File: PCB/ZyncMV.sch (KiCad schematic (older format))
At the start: 0 parts

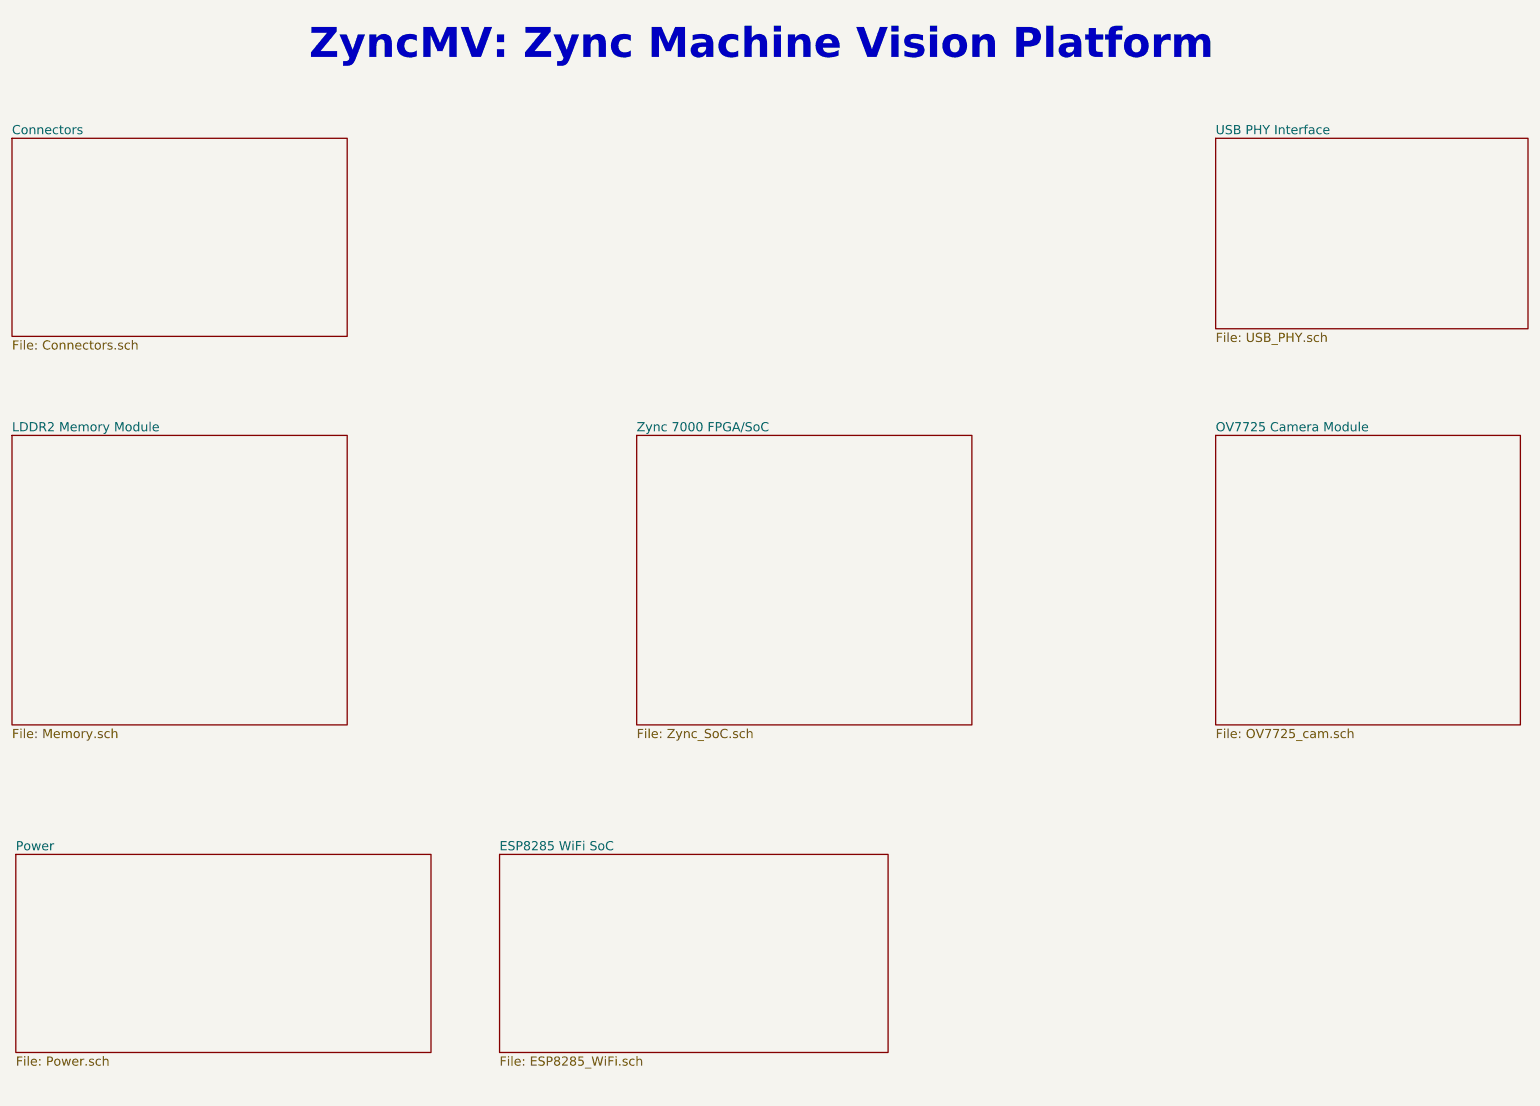
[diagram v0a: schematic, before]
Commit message: Progress
Datasheets added for regulators, regulators chosen, more datasheets
ralted to Zync 7000 added. Memory module chose footprint created and
datasheet added. Schematic work in progress. Project is slow going do to
th sheer amount of documenation to absorb on the Zync and makign high
pin count BGAs is tedious. More to follow soon.
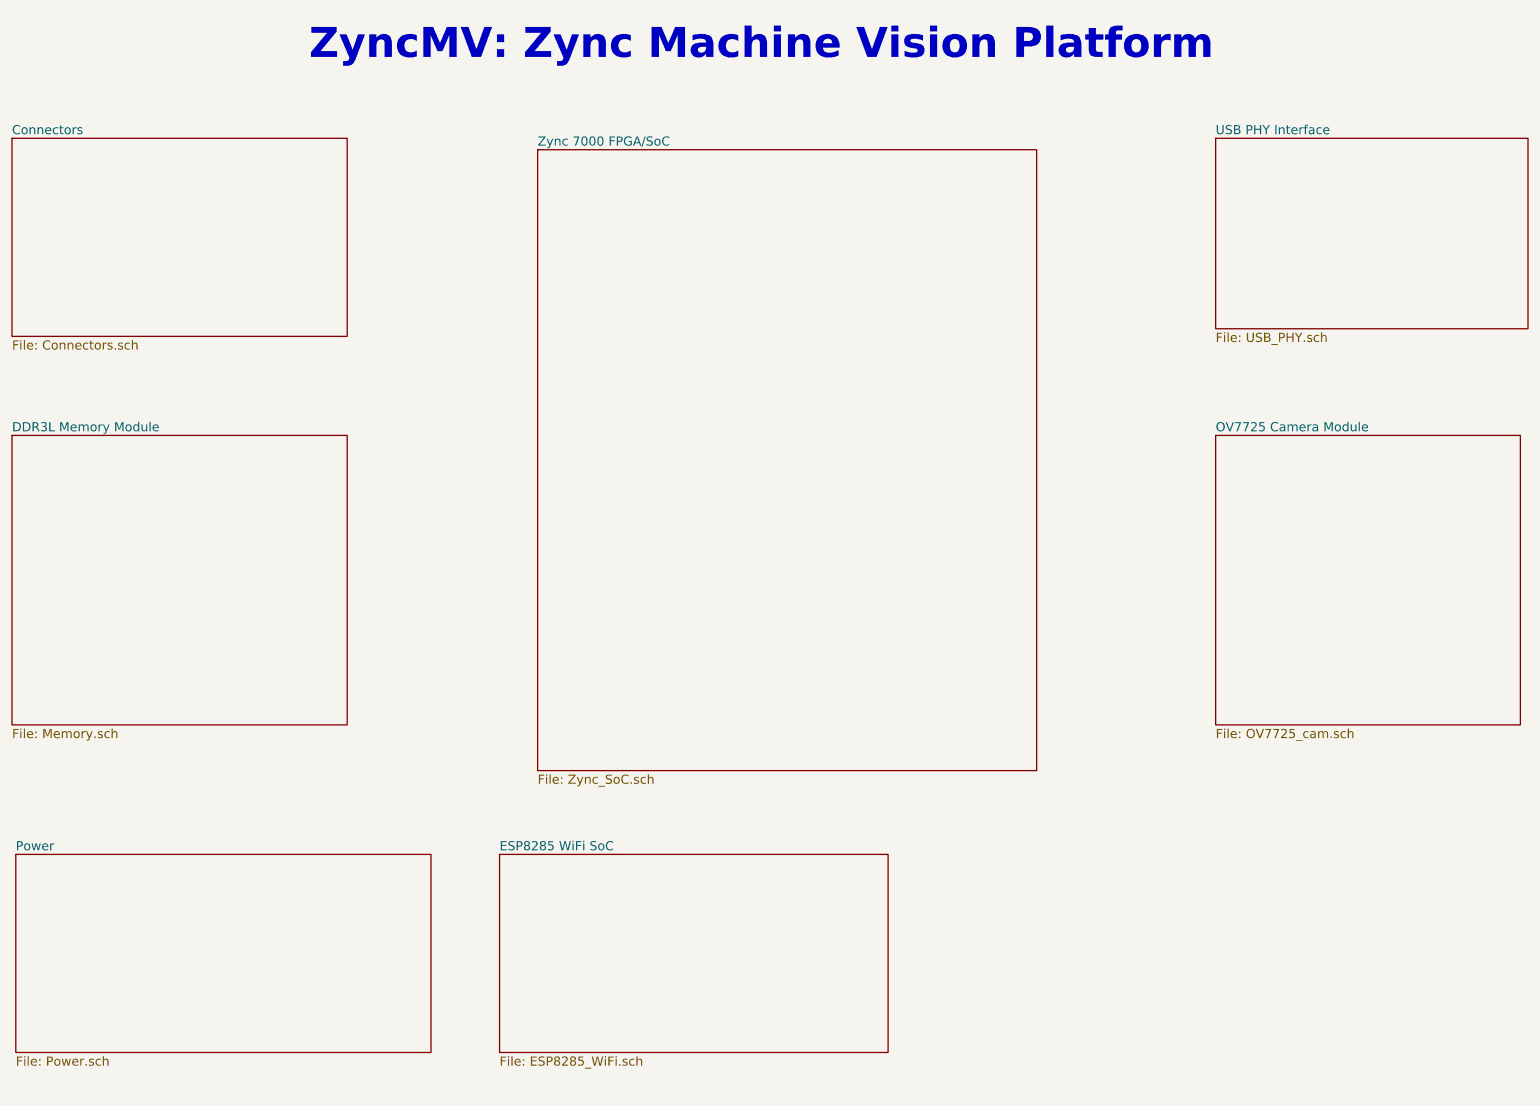
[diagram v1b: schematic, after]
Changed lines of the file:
@@
 LIBS:HydroPWNics_Lib
 LIBS:OnHand-Components-Sym
+LIBS:ZyncMV-cache
 EELAYER 25 0
 EELAYER END
 $Descr A4 11693 8268
 encoding utf-8
-Sheet 1 11
+Sheet 1 8
 Title ""
 Date ""
@@
 $EndDescr
 $Sheet
-S 5000 3450 2200 1900
+S 4350 1575 3275 4075
 U 585AE0B8
 F0 "Zync 7000 FPGA/SoC" 60
@@
 S 900  3450 2200 1900
 U 585AE128
-F0 "LDDR2 Memory Module" 60
+F0 "DDR3L Memory Module" 60
 F1 "Memory.sch" 60
 $EndSheet

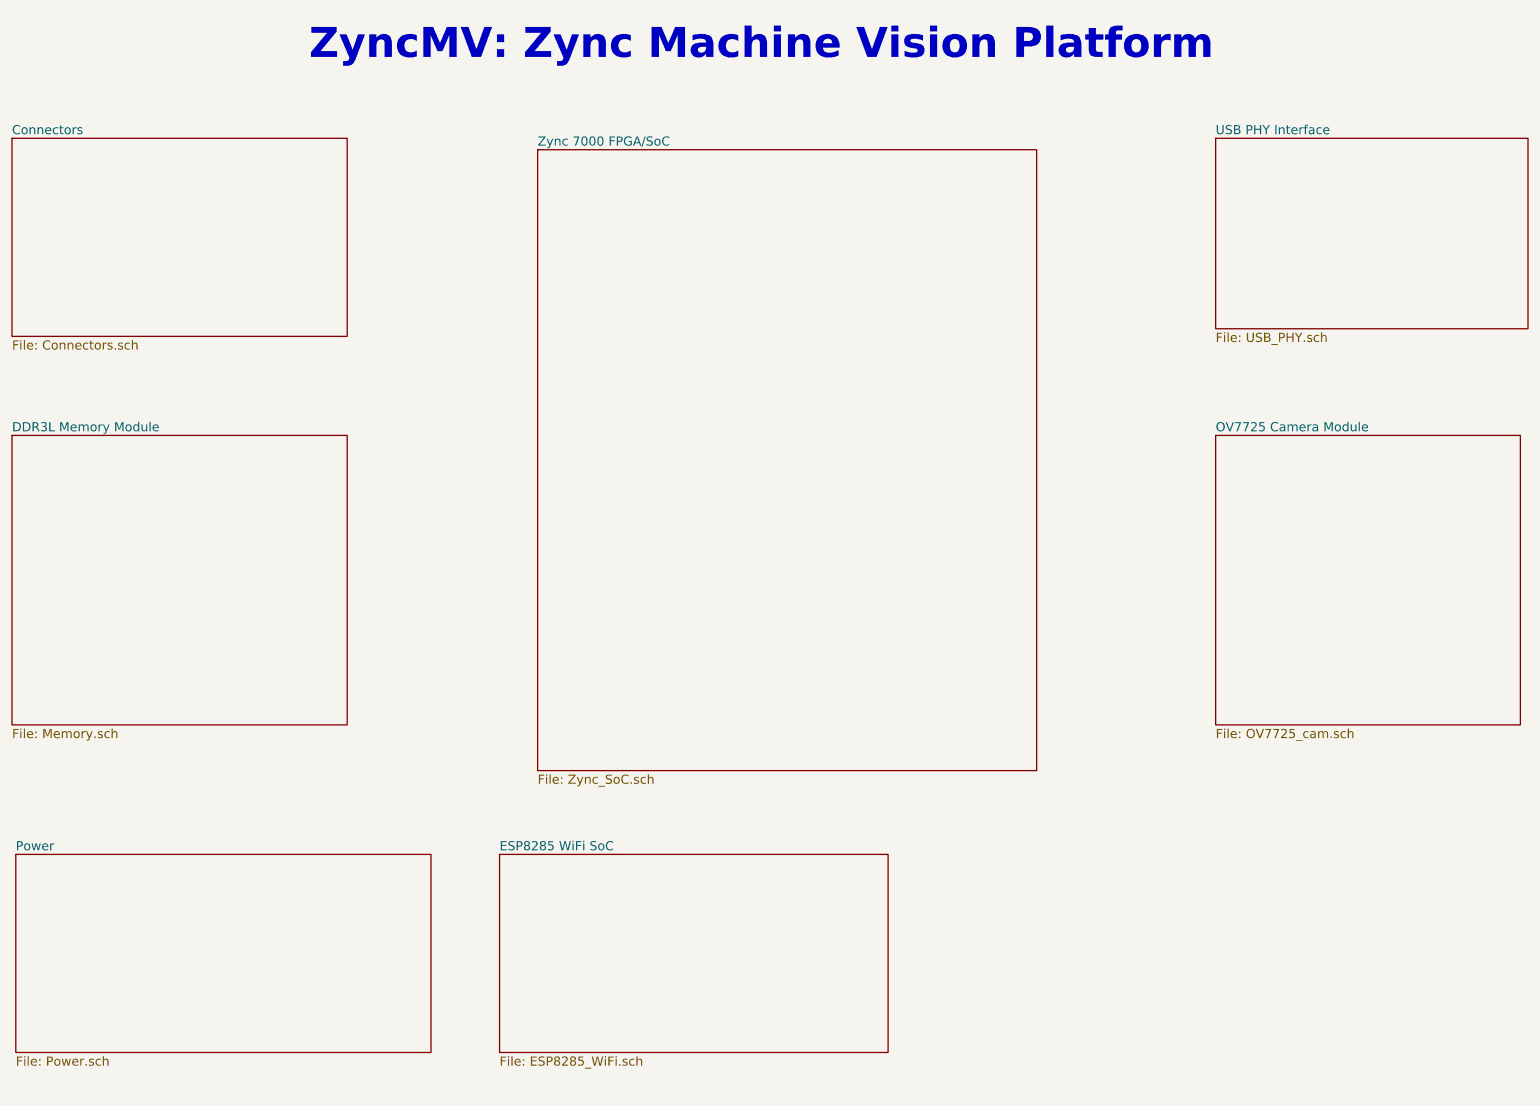
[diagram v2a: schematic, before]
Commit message: Power
Power topology change. Power system schematic spans 3 pages. two for the
PMIC that supplies the SoC and the DDR3L and an addional page covering
input stage and DCDC regulators for other voltages, particularly for the
off board lighting module.
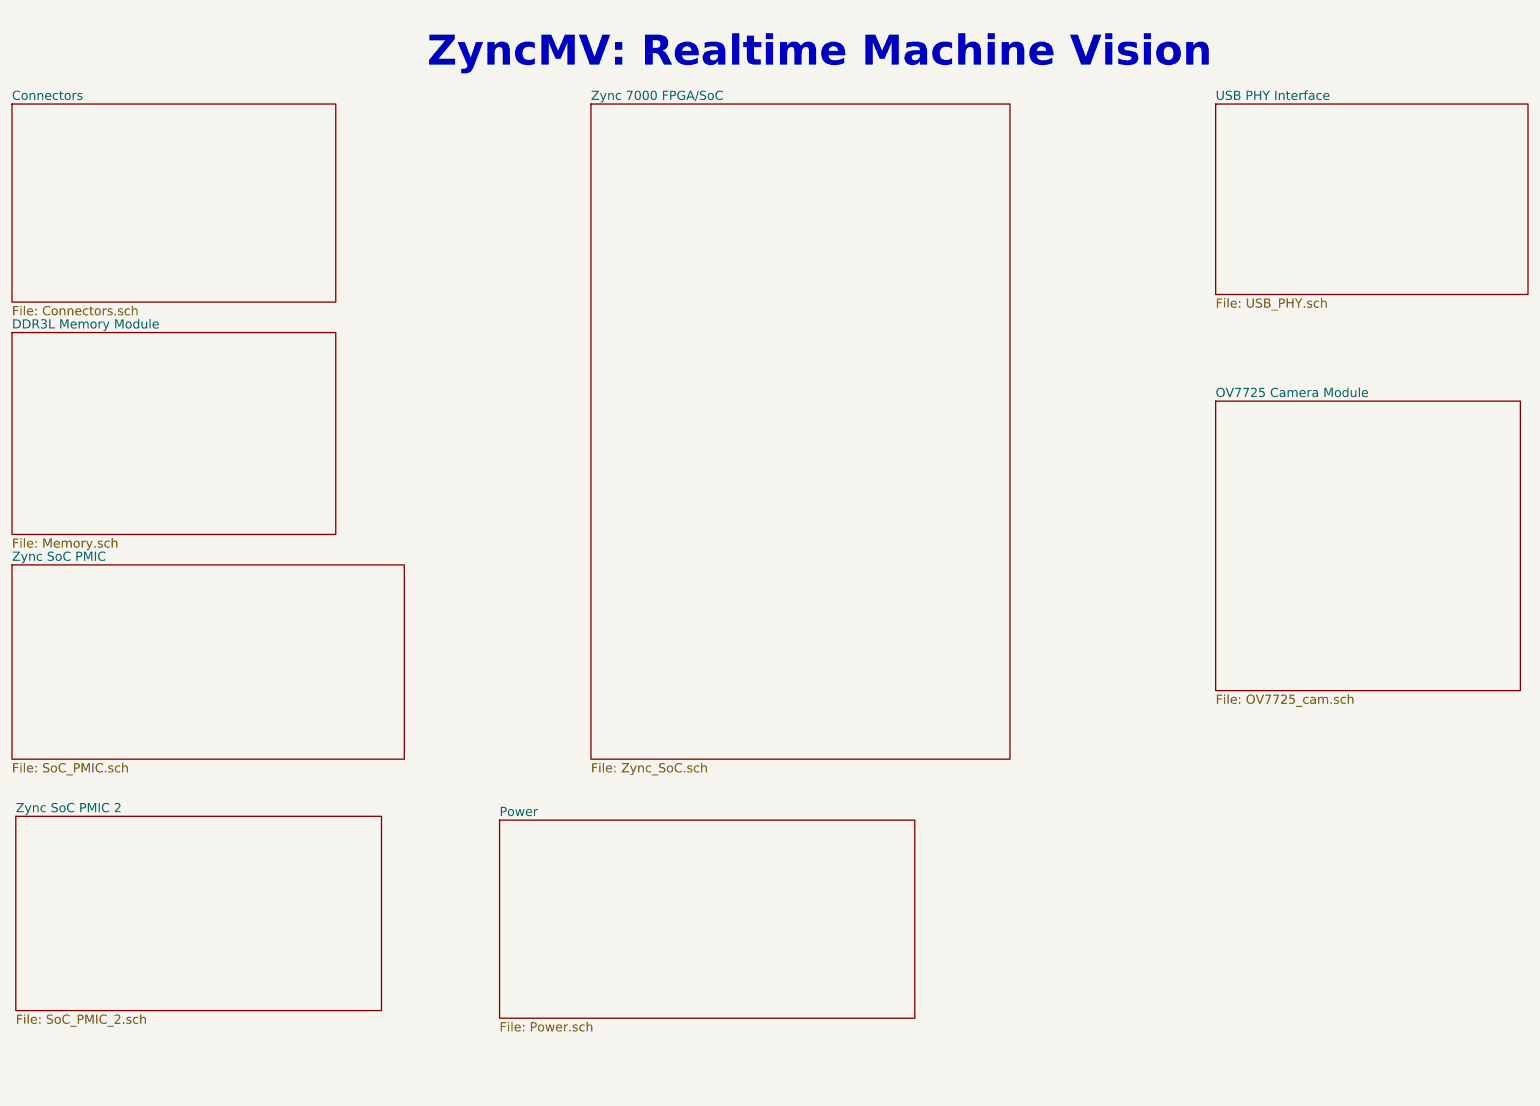
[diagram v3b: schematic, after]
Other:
- note added: "ZyncMV: Realtime Machine Vision"
- note removed: "ZyncMV: Zync Machine Vision Platform"
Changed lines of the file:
@@
 $Descr A4 11693 8268
 encoding utf-8
-Sheet 1 8
+Sheet 1 9
 Title ""
 Date "2016-12-23"
@@
 $EndDescr
 $Sheet
-S 4350 1575 3275 4075
+S 4700 1275 2750 4300
 U 585AE0B8
 F0 "Zync 7000 FPGA/SoC" 60
@@
 $EndSheet
 $Sheet
-S 925  6200 2725 1300
+S 4100 5975 2725 1300
 U 585AE0DE
 F0 "Power" 60
@@
 $EndSheet
 $Sheet
-S 8800 3450 2000 1900
+S 8800 3225 2000 1900
 U 585AE0EB
 F0 "OV7725 Camera Module" 60
@@
 $EndSheet
 $Sheet
-S 4100 6200 2550 1300
-U 585AE108
-F0 "ESP8285 WiFi SoC" 60
-F1 "ESP8285_WiFi.sch" 60
-$EndSheet
-$Sheet
-S 900  3450 2200 1900
+S 900  2775 2125 1325
 U 585AE128
 F0 "DDR3L Memory Module" 60
@@
 $EndSheet
 $Sheet
-S 900  1500 2200 1300
+S 900  1275 2125 1300
 U 585AE13E
 F0 "Connectors" 60
@@
 $EndSheet
 $Sheet
-S 8800 1500 2050 1250
+S 8800 1275 2050 1250
 U 585AE27C
 F0 "USB PHY Interface" 60
 F1 "USB_PHY.sch" 60
 $EndSheet
-Text Notes 2850 1000 0    197  ~ 39
-ZyncMV: Zync Machine Vision Platform
+Text Notes 3625 1050 0    197  ~ 39
+ZyncMV: Realtime Machine Vision
+$Sheet
+S 900  4300 2575 1275
+U 5878744A
+F0 "Zync SoC PMIC" 60
+F1 "SoC_PMIC.sch" 60
+$EndSheet
+$Sheet
+S 925  5950 2400 1275
+U 5878DB5C
+F0 "Zync SoC PMIC 2" 60
+F1 "SoC_PMIC_2.sch" 60
+$EndSheet
 $EndSCHEMATC

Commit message: DDR3L
major progress on DDR3L schematic. Still need to edit bus enries and
make control signals their own entry each.
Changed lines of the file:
@@
 LIBS:xilinx6s
 LIBS:xilinx6v
-LIBS:xilinx7
 LIBS:xilinxultra
 LIBS:HydroPWNics_Lib
@@
 F0 "DDR3L Memory Module" 60
 F1 "Memory.sch" 60
+F2 "MEM_DATA_BUS" B R 3025 3100 60
+F3 "MEM_ADDR_BUS" B R 3025 3325 60
+F4 "CTRL_SIG_BUS" B R 3025 3475 60
+F5 "DDR3L_VREF" B R 3025 3650 60
 $EndSheet
 $Sheet

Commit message: Cam / PMIC
Camera data bus entry relabled, PMIC started.
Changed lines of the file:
@@
 $EndSheet
 $Sheet
-S 4100 5975 2725 1300
+S 4125 6925 975  375
 U 585AE0DE
 F0 "Power" 60

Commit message: Schematic Progress
More progress on schematic. Image sensor schematic nearly finished, need
to check termination requirements of signals. Memory schematic nearly
solidified. LDO added to image sensor circuit for analog supply (3V).
Need to research termination requirements for memory as well. Need to
check what internal termination if any resistors are available in the
Zynq soc.
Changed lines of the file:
@@
 S 8800 3225 2000 1900
 U 585AE0EB
-F0 "OV7725 Camera Module" 60
-F1 "OV7725_cam.sch" 60
+F0 "OV04689-H67A CMOS Image Sensor" 60
+F1 "OV04689_H67A.sch" 60
 $EndSheet
 $Sheet
